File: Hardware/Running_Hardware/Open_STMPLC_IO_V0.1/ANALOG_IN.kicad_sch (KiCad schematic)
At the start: 67 parts, among them J35 Screw_Terminal_01x03, J36 Screw_Terminal_01x03, J37 Screw_Terminal_01x03, J38 Screw_Terminal_01x03, U39 AD4111, U40 REF3025, Y2 16MHz

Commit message: New DXF update
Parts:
- J35, J36, J37, J38: footprint TerminalBlock_Phoenix:TerminalBlock_Phoenix_MKDS-1,5-3-5.08_1x03_P5.08mm_Horizontal -> TerminalBlock_Phoenix:TerminalBlock_Phoenix_MKDS-1-3-3.81_1x03_P3.81mm_Horizontal
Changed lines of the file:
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@@
 		)
 		(instances
-			(project ""
+			(project "Open_STMPLC_IO_V0.1"
 				(path "/4d6787b6-1f4f-4098-b70b-d936e584350b/9484d068-112e-4f97-bb8e-f93d2b86f9c0"
 					(reference "U39")
@@
 			)
 		)
-		(property "Footprint" "TerminalBlock_Phoenix:TerminalBlock_Phoenix_MKDS-1,5-3-5.08_1x03_P5.08mm_Horizontal"
+		(property "Footprint" "TerminalBlock_Phoenix:TerminalBlock_Phoenix_MKDS-1-3-3.81_1x03_P3.81mm_Horizontal"
 			(at 257.81 113.03 0)
 			(effects
@@
 			)
 		)
-		(property "Footprint" "TerminalBlock_Phoenix:TerminalBlock_Phoenix_MKDS-1,5-3-5.08_1x03_P5.08mm_Horizontal"
+		(property "Footprint" "TerminalBlock_Phoenix:TerminalBlock_Phoenix_MKDS-1-3-3.81_1x03_P3.81mm_Horizontal"
 			(at 257.81 54.61 0)
 			(effects
@@
 		)
 		(instances
-			(project ""
+			(project "Open_STMPLC_IO_V0.1"
 				(path "/4d6787b6-1f4f-4098-b70b-d936e584350b/9484d068-112e-4f97-bb8e-f93d2b86f9c0"
 					(reference "D126")
@@
 		)
 		(instances
-			(project ""
+			(project "Open_STMPLC_IO_V0.1"
 				(path "/4d6787b6-1f4f-4098-b70b-d936e584350b/9484d068-112e-4f97-bb8e-f93d2b86f9c0"
 					(reference "U40")
@@
 		)
 		(instances
-			(project ""
+			(project "Open_STMPLC_IO_V0.1"
 				(path "/4d6787b6-1f4f-4098-b70b-d936e584350b/9484d068-112e-4f97-bb8e-f93d2b86f9c0"
 					(reference "F1")
@@
 			)
 		)
-		(property "Footprint" "TerminalBlock_Phoenix:TerminalBlock_Phoenix_MKDS-1,5-3-5.08_1x03_P5.08mm_Horizontal"
+		(property "Footprint" "TerminalBlock_Phoenix:TerminalBlock_Phoenix_MKDS-1-3-3.81_1x03_P3.81mm_Horizontal"
 			(at 181.61 113.03 0)
 			(effects
@@
 		)
 		(instances
-			(project ""
+			(project "Open_STMPLC_IO_V0.1"
 				(path "/4d6787b6-1f4f-4098-b70b-d936e584350b/9484d068-112e-4f97-bb8e-f93d2b86f9c0"
 					(reference "TP1")
@@
 			)
 		)
-		(property "Footprint" "TerminalBlock_Phoenix:TerminalBlock_Phoenix_MKDS-1,5-3-5.08_1x03_P5.08mm_Horizontal"
+		(property "Footprint" "TerminalBlock_Phoenix:TerminalBlock_Phoenix_MKDS-1-3-3.81_1x03_P3.81mm_Horizontal"
 			(at 181.61 54.61 0)
 			(effects
@@
 		)
 		(instances
-			(project ""
+			(project "Open_STMPLC_IO_V0.1"
 				(path "/4d6787b6-1f4f-4098-b70b-d936e584350b/9484d068-112e-4f97-bb8e-f93d2b86f9c0"
 					(reference "J35")

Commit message: IO board layout 1
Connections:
- net GND: now also J35.3 (Pin_3), J36.3 (Pin_3), J37.3 (Pin_3), J38.3 (Pin_3); no longer J35.1 (Pin_1), J36.1 (Pin_1), J37.1 (Pin_1), J38.1 (Pin_1)
- net at F3.1: now also J37.1 (Pin_1); no longer J37.3 (Pin_3)
- net at F4.1: now also J38.1 (Pin_1); no longer J38.3 (Pin_3)
- net at F2.1: now also J36.1 (Pin_1); no longer J36.3 (Pin_3)
- net at F1.1: now also J35.1 (Pin_1); no longer J35.3 (Pin_3)
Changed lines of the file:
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@@
 		(lib_id "Connector:Screw_Terminal_01x03")
 		(at 257.81 113.03 0)
-		(mirror x)
 		(unit 1)
 		(exclude_from_sim no)
@@
 		(dnp no)
 		(property "Reference" "J38"
-			(at 257.81 104.902 0)
+			(at 257.81 121.158 0)
 			(effects
 				(font
@@
 		)
 		(property "Value" "Screw_Terminal_01x03"
-			(at 261.366 107.188 0)
+			(at 261.366 118.872 0)
 			(effects
 				(font
@@
 		(lib_id "Connector:Screw_Terminal_01x03")
 		(at 257.81 54.61 0)
-		(mirror x)
 		(unit 1)
 		(exclude_from_sim no)
@@
 		(dnp no)
 		(property "Reference" "J36"
-			(at 257.81 46.482 0)
+			(at 257.81 62.738 0)
 			(effects
 				(font
@@
 		)
 		(property "Value" "Screw_Terminal_01x03"
-			(at 261.366 48.768 0)
+			(at 261.366 60.452 0)
 			(effects
 				(font
@@
 		(lib_id "Connector:Screw_Terminal_01x03")
 		(at 181.61 113.03 0)
-		(mirror x)
 		(unit 1)
 		(exclude_from_sim no)
@@
 		(dnp no)
 		(property "Reference" "J37"
-			(at 181.61 104.902 0)
+			(at 181.61 121.158 0)
 			(effects
 				(font
@@
 		)
 		(property "Value" "Screw_Terminal_01x03"
-			(at 185.166 107.188 0)
+			(at 185.166 118.872 0)
 			(effects
 				(font
@@
 		(lib_id "Connector:Screw_Terminal_01x03")
 		(at 181.61 54.61 0)
-		(mirror x)
 		(unit 1)
 		(exclude_from_sim no)
@@
 		(dnp no)
 		(property "Reference" "J35"
-			(at 181.61 46.482 0)
+			(at 181.61 62.738 0)
 			(effects
 				(font
@@
 		)
 		(property "Value" "Screw_Terminal_01x03"
-			(at 185.166 48.768 0)
+			(at 185.166 60.452 0)
 			(effects
 				(font

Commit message: IO board layout
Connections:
- net ANALOG_IN_ERROR: now reaches D126.1 (K), U39.18 (~{ERROR})
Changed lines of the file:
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@@
+	)
+	(junction
+		(at 102.87 69.85)
+		(diameter 0)
+		(color 0 0 0 0)
 	)
 	(junction
@@
 		(pts
 			(xy 100.33 109.22) (xy 100.33 107.95)
+		)
+		(stroke
+			(width 0)
+			(type default)
+		)
+	)
+	(wire
+		(pts
+			(xy 102.87 69.85) (xy 111.76 69.85)
 		)
 		(stroke
@@
 		)
 	)
+	(hierarchical_label "ANALOG_IN_ERROR"
+		(shape output)
+		(at 111.76 69.85 0)
+		(effects
+			(font
+				(size 1 1)
+			)
+			(justify left)
+		)
+	)

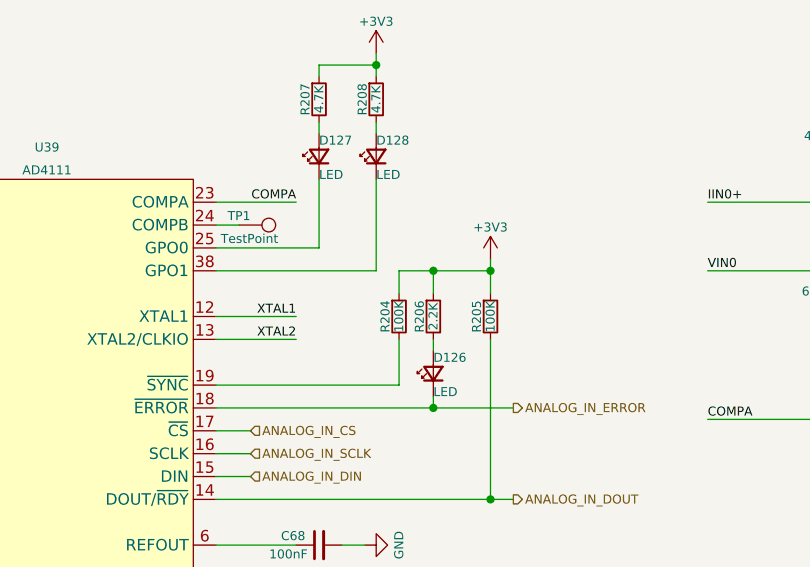
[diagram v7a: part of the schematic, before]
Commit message: Schematic updates
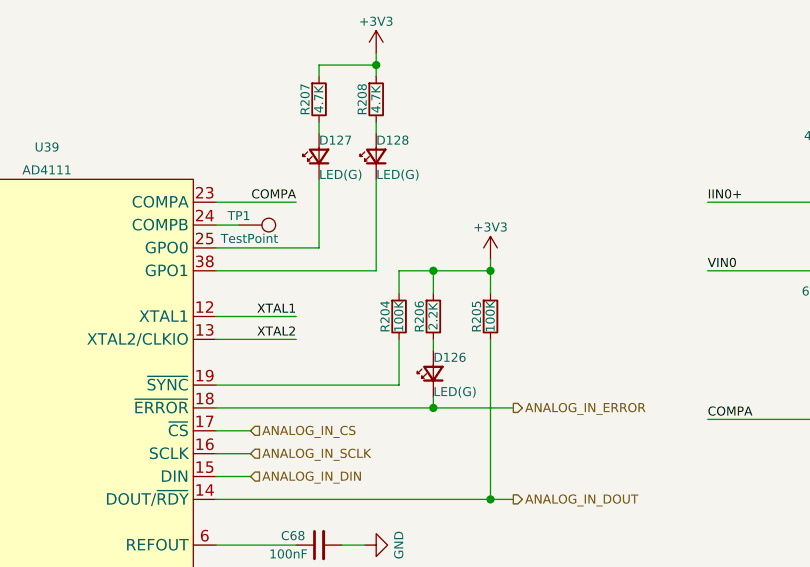
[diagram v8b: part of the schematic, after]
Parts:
- D126, D127, D128: value LED -> LED(G)
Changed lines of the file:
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@@
 			)
 		)
-		(property "Value" "LED"
+		(property "Value" "LED(G)"
 			(at 96.52 43.942 90)
 			(effects
@@
 			)
 		)
-		(property "Value" "LED"
+		(property "Value" "LED(G)"
 			(at 102.87 68.072 90)
 			(effects
@@
 			)
 		)
-		(property "Value" "LED"
+		(property "Value" "LED(G)"
 			(at 90.17 43.942 90)
 			(effects
